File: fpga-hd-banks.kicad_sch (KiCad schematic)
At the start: 16 parts, among them Q4 BSS138PW, Q5 BSS138PW, Q6 BSS138PW, Q7 BSS138PW, Q8 BSS138PW, U34 XCAU25P-2FFVB676I

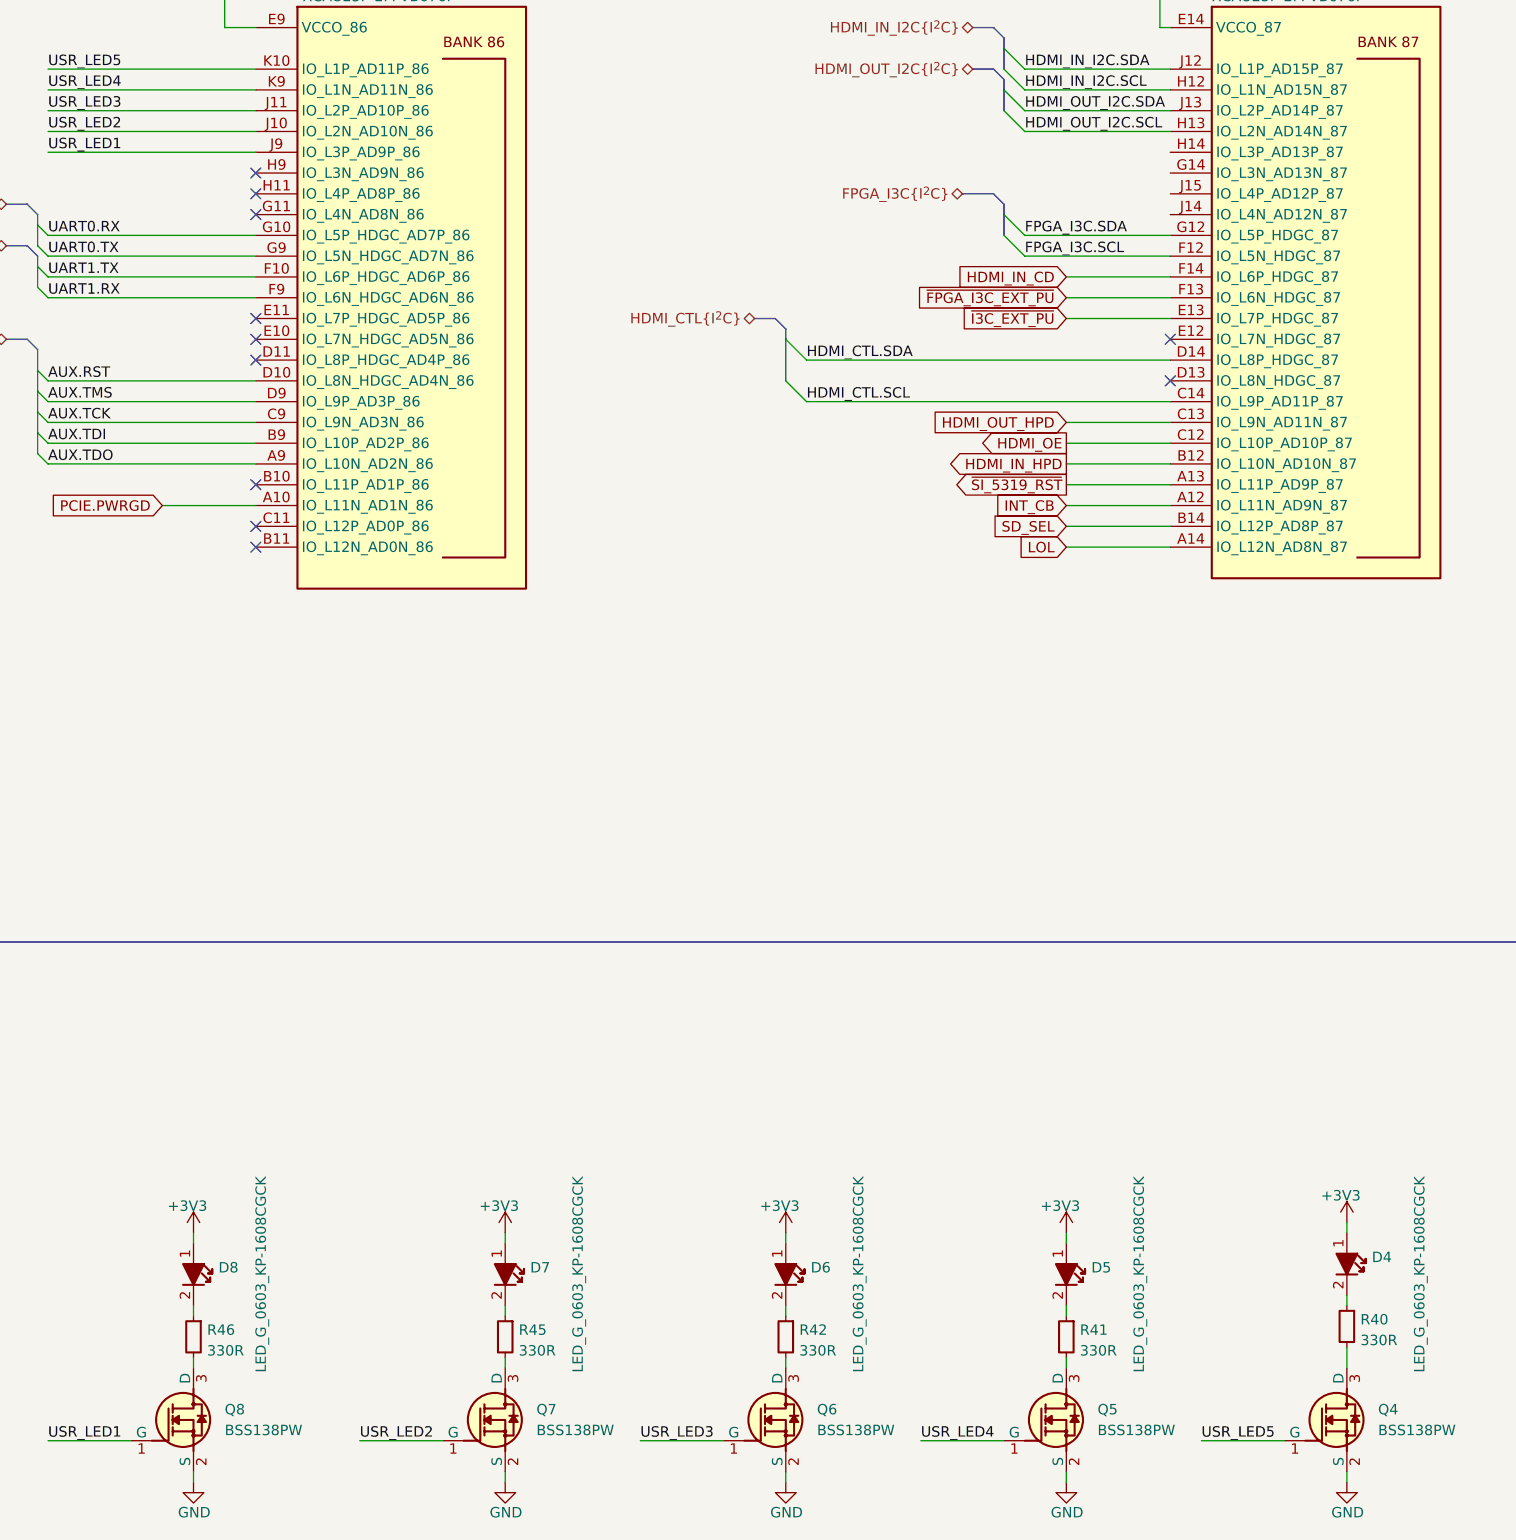
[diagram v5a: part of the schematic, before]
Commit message: [#68016] Solve ERC warrings and errors
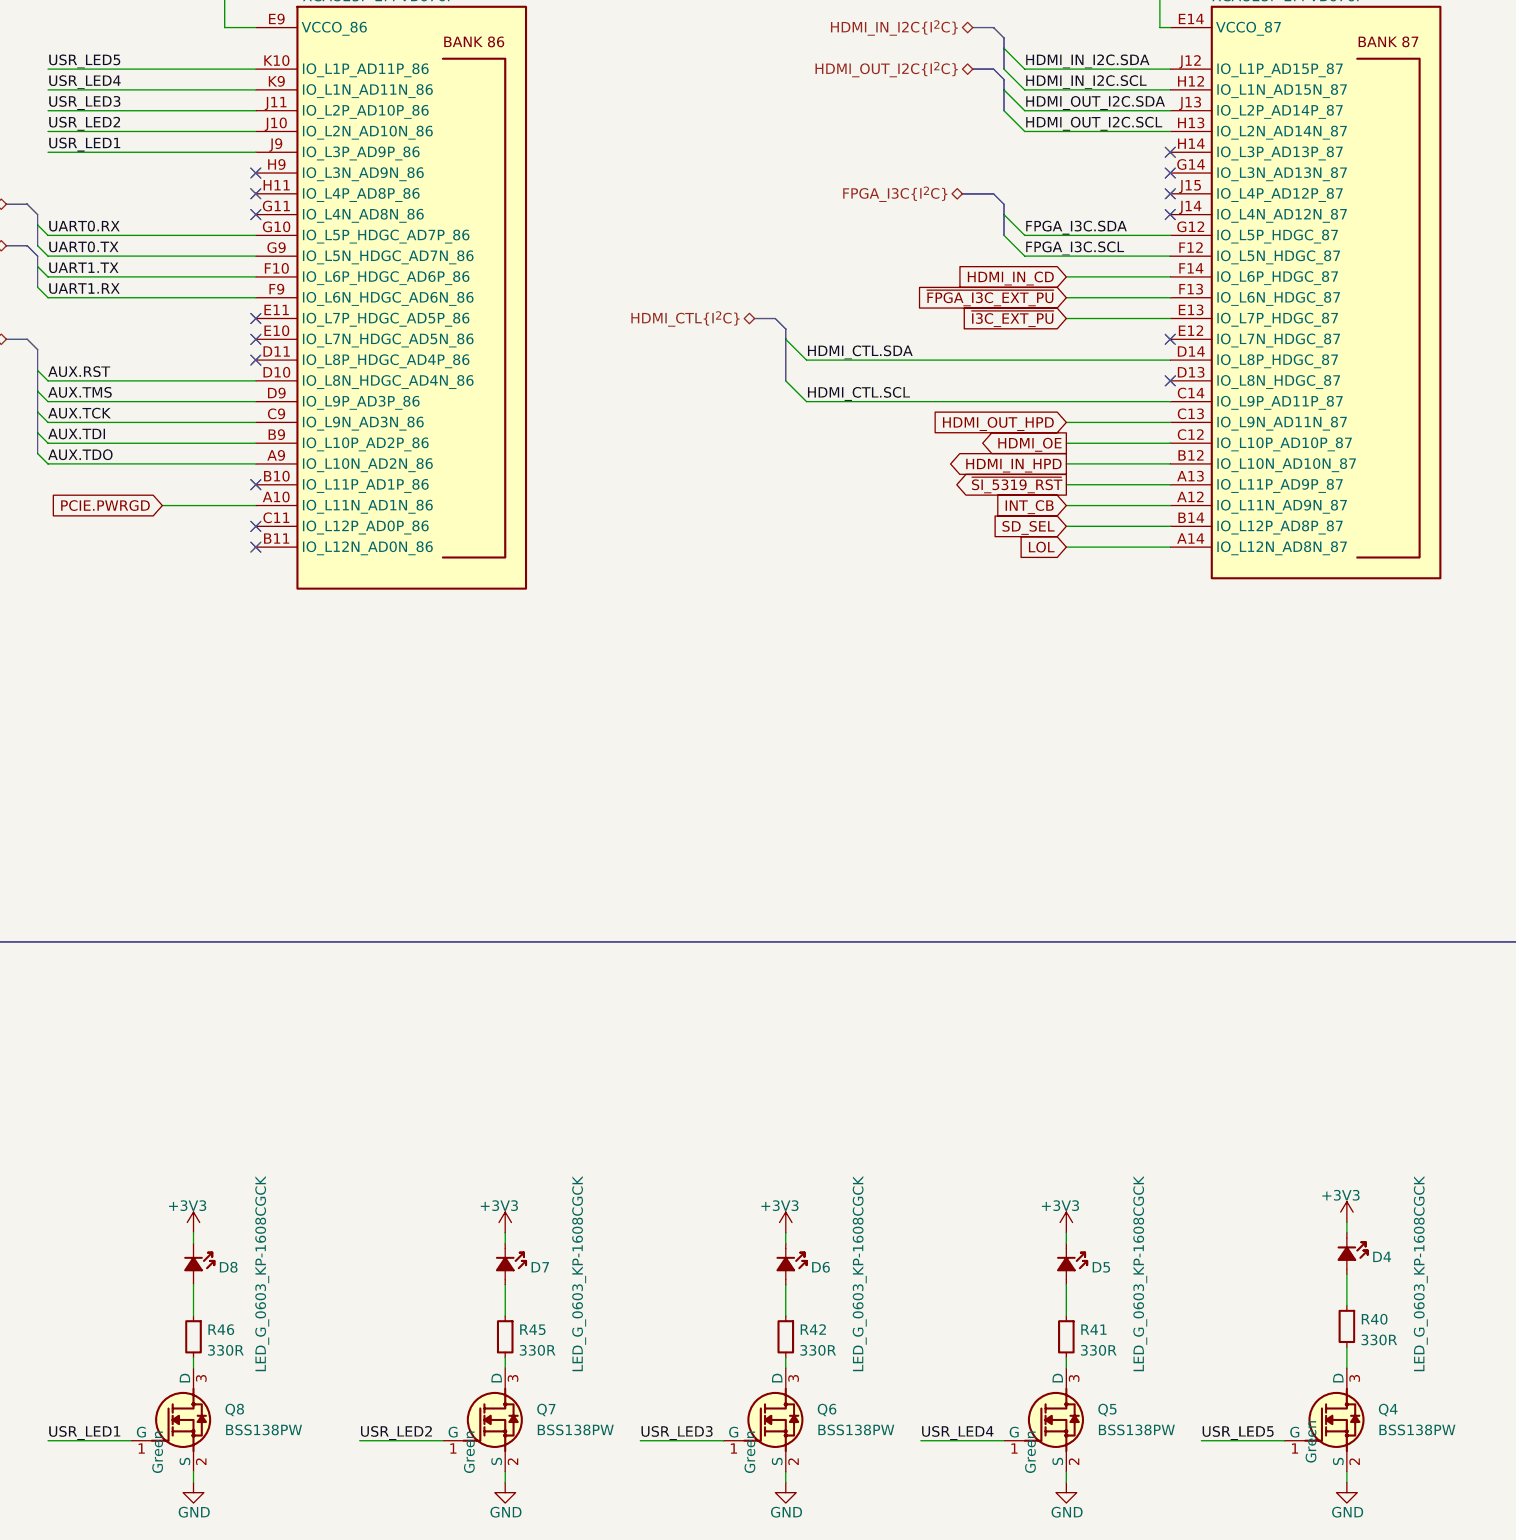
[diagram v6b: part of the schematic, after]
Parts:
- D4, D5, D6, D7, D8: Color (none) -> Green
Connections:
- no-connect marks 20 -> 24
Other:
- moved on the sheet: D4, D5, D6, D7, D8
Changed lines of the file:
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@@
   (no_connect (at 93.98 110.49))
   (no_connect (at 93.98 107.95))
+  (no_connect (at 205.74 90.17))
+  (no_connect (at 205.74 87.63))
   (no_connect (at 318.77 118.11))
   (no_connect (at 93.98 128.27))
@@
   (no_connect (at 93.98 92.71))
   (no_connect (at 318.77 102.87))
+  (no_connect (at 205.74 92.71))
+  (no_connect (at 205.74 95.25))
   (no_connect (at 318.77 105.41))
   (no_connect (at 318.77 97.79))
@@
     (stroke (width 0) (type default))
   )
-  (wire (pts (xy 158.75 228.6) (xy 158.75 229.87))
+  (wire (pts (xy 158.75 226.06) (xy 158.75 229.87))
     (stroke (width 0) (type default))
   )
@@
     (stroke (width 0) (type default))
   )
-  (wire (pts (xy 86.36 228.6) (xy 86.36 229.87))
+  (wire (pts (xy 86.36 226.06) (xy 86.36 229.87))
     (stroke (width 0) (type default))
   )
@@
     (stroke (width 0) (type default))
   )
+  (wire (pts (xy 124.46 226.06) (xy 124.46 229.87))
+    (stroke (width 0) (type default))
+  )
   (wire (pts (xy 292.1 95.25) (xy 318.77 95.25))
     (stroke (width 0) (type default))
@@
     (stroke (width 0) (type default))
   )
-  (wire (pts (xy 124.46 228.6) (xy 124.46 229.87))
-    (stroke (width 0) (type default))
-  )
-  (wire (pts (xy 193.04 228.6) (xy 193.04 229.87))
+  (wire (pts (xy 193.04 226.06) (xy 193.04 229.87))
     (stroke (width 0) (type default))
   )
@@
     (stroke (width 0) (type default))
   )
-  (wire (pts (xy 227.33 227.33) (xy 227.33 228.6))
+  (wire (pts (xy 227.33 224.79) (xy 227.33 228.6))
     (stroke (width 0) (type default))
   )
@@
       (effects (font (size 1.27 1.27) (thickness 0.15)) (justify left bottom) hide)
     )
-    (property "Datasheet" "http://www.farnell.com/datasheets/2045956.pdf" (at 214.63 242.57 0)
+    (property "Datasheet" "http://www.kingbright.com/attachments/file/psearch//000/00/00/KP-1608CGCK(Ver.23B).pdf" (at 214.63 242.57 0)
       (effects (font (size 1.27 1.27) (thickness 0.15)) (justify left bottom) hide)
     )
@@
     (property "License" "Apache-2.0" (at 204.47 242.57 0)
       (effects (font (size 1.27 1.27) (thickness 0.15)) (justify left bottom) hide)
+    )
+    (property "Color" "Green" (at 222.25 242.57 0)
+      (effects (font (size 1.27 1.27)) (justify left bottom))
     )
     (pin "1")
@@
       (effects (font (size 1.27 1.27) (thickness 0.15)) (justify left bottom) hide)
     )
-    (property "Datasheet" "http://www.farnell.com/datasheets/2045956.pdf" (at 180.34 243.84 0)
+    (property "Datasheet" "http://www.kingbright.com/attachments/file/psearch//000/00/00/KP-1608CGCK(Ver.23B).pdf" (at 180.34 243.84 0)
       (effects (font (size 1.27 1.27) (thickness 0.15)) (justify left bottom) hide)
     )
@@
     (property "License" "Apache-2.0" (at 170.18 243.84 0)
       (effects (font (size 1.27 1.27) (thickness 0.15)) (justify left bottom) hide)
+    )
+    (property "Color" "Green" (at 187.96 243.84 0)
+      (effects (font (size 1.27 1.27)) (justify left bottom))
     )
     (pin "1")
@@
       (effects (font (size 1.27 1.27) (thickness 0.15)) (justify left bottom) hide)
     )
-    (property "Datasheet" "http://www.farnell.com/datasheets/2045956.pdf" (at 111.76 243.84 0)
+    (property "Datasheet" "http://www.kingbright.com/attachments/file/psearch//000/00/00/KP-1608CGCK(Ver.23B).pdf" (at 111.76 243.84 0)
       (effects (font (size 1.27 1.27) (thickness 0.15)) (justify left bottom) hide)
     )
@@
     (property "License" "Apache-2.0" (at 101.6 243.84 0)
       (effects (font (size 1.27 1.27) (thickness 0.15)) (justify left bottom) hide)
+    )
+    (property "Color" "Green" (at 119.38 243.84 0)
+      (effects (font (size 1.27 1.27)) (justify left bottom))
     )
     (pin "1")
@@
       (effects (font (size 1.27 1.27) (thickness 0.15)) (justify left bottom) hide)
     )
-    (property "Datasheet" "http://www.farnell.com/datasheets/2045956.pdf" (at 73.66 243.84 0)
+    (property "Datasheet" "http://www.kingbright.com/attachments/file/psearch//000/00/00/KP-1608CGCK(Ver.23B).pdf" (at 73.66 243.84 0)
       (effects (font (size 1.27 1.27) (thickness 0.15)) (justify left bottom) hide)
     )
@@
     (property "License" "Apache-2.0" (at 63.5 243.84 0)
       (effects (font (size 1.27 1.27) (thickness 0.15)) (justify left bottom) hide)
+    )
+    (property "Color" "Green" (at 81.28 243.84 0)
+      (effects (font (size 1.27 1.27)) (justify left bottom))
     )
     (pin "1")
@@
       (effects (font (size 1.27 1.27) (thickness 0.15)) (justify left bottom) hide)
     )
-    (property "Datasheet" "http://www.farnell.com/datasheets/2045956.pdf" (at 146.05 243.84 0)
+    (property "Datasheet" "http://www.kingbright.com/attachments/file/psearch//000/00/00/KP-1608CGCK(Ver.23B).pdf" (at 146.05 243.84 0)
       (effects (font (size 1.27 1.27) (thickness 0.15)) (justify left bottom) hide)
     )
@@
     (property "License" "Apache-2.0" (at 135.89 243.84 0)
       (effects (font (size 1.27 1.27) (thickness 0.15)) (justify left bottom) hide)
+    )
+    (property "Color" "Green" (at 153.67 243.84 0)
+      (effects (font (size 1.27 1.27)) (justify left bottom))
     )
     (pin "1")
@@
     )
   )
-  (symbol (lib_id "antmicroFPGAChips:XCAU25P-2FFVB676I") (at 205.74 72.39 0) (unit 8)
+  (symbol (lib_name "XCAU25P-2FFVB676I_1") (lib_id "antmicroFPGAChips:XCAU25P-2FFVB676I") (at 205.74 72.39 0) (unit 8)
     (in_bom yes) (on_board yes) (dnp no)
     (property "Reference" "U34" (at 210.82 66.04 0)
@@
     )
   )
-  (symbol (lib_id "antmicroFPGAChips:XCAU25P-2FFVB676I") (at 318.77 72.39 0) (unit 6)
+  (symbol (lib_name "XCAU25P-2FFVB676I_2") (lib_id "antmicroFPGAChips:XCAU25P-2FFVB676I") (at 318.77 72.39 0) (unit 6)
     (in_bom yes) (on_board yes) (dnp no)
     (property "Reference" "U34" (at 324.485 66.04 0)

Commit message: [#68088] Add heater connector
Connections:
- net Heater_PWM: now reaches U34.AB16 (IO_L6N_HDGC_AD6N_84)
- no-connect marks 24 -> 23
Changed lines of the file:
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@@
   (no_connect (at 205.74 92.71))
   (no_connect (at 205.74 95.25))
-  (no_connect (at 318.77 105.41))
   (no_connect (at 318.77 97.79))
   (no_connect (at 93.98 95.25))
@@
     (stroke (width 0) (type default))
   )
+  (wire (pts (xy 292.1 105.41) (xy 318.77 105.41))
+    (stroke (width 0) (type default))
+  )
   (wire (pts (xy 292.1 107.95) (xy 318.77 107.95))
     (stroke (width 0) (type default))
@@
       (effects (font (size 1.27 1.27)) (justify right))
     )
+  )
+  (global_label "Heater_PWM" (shape input) (at 292.1 105.41 180) (fields_autoplaced)
+    (effects (font (size 1.27 1.27)) (justify right))
+    (property "Intersheetrefs" "${INTERSHEET_REFS}" (at 278.46 105.41 0)
+      (effects (font (size 1.27 1.27)) (justify right))
+    )
